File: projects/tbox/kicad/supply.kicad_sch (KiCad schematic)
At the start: 38 parts, among them J2501 PWR IN (panel Powerpole), U2501 ADP7142AUJZ-5.0, U2502 OPA1678, U2503 TPS7A4701, U2504 TPS3808G01

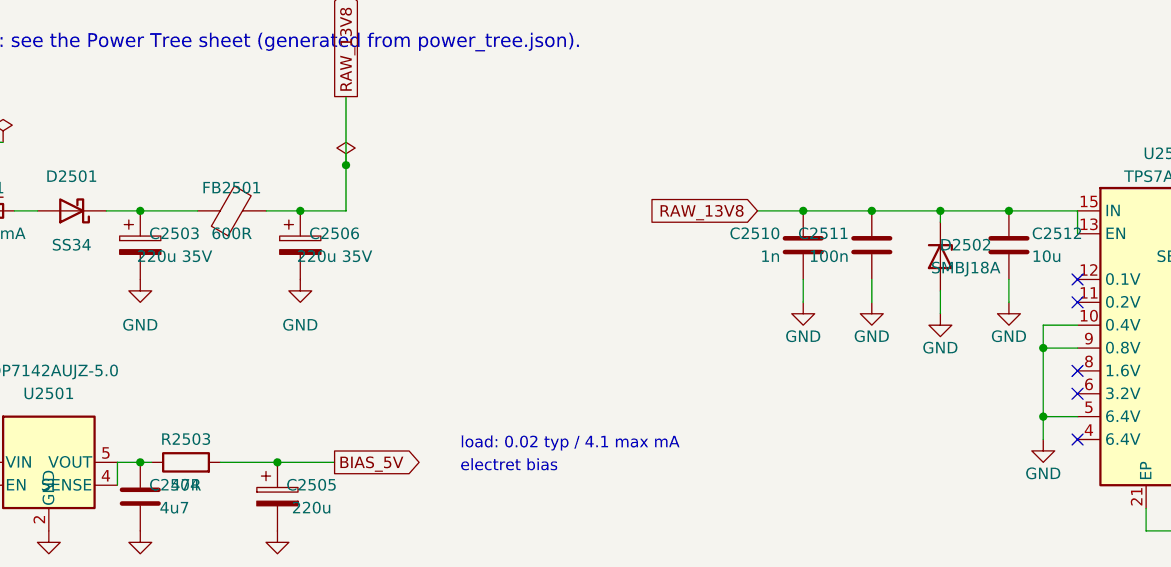
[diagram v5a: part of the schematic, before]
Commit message: Review 2 design decisions: mute cell sequencing, phones precharge, non-inverting BLEND, chassis RF returns, SP724 bypass and placement, TVS ahead of the bead, load and level updates
Q1  Mute cell: MUTE is a source-only OR with a 100k pull-down; a 2N7002
    inverter (Q1203) and sink (Q1204) pull SW_CTL hard low on release so
    the SPDT reconnects under the shunt, the fade gate charges through
    D1201/47k and bleeds through 470k (~50 ms); nothing discharges
    through MUTE any more.
Q2  1k from Vref on each OPA1622 output node (R2425-R2428) precharges
    the 470u phones caps during the hold.
Q3  Fade resistor 220R (all three instances): 0.2 dB insertion, TX_MIX
    level within 0.3 dB of the line-out jumpering.
Q4  LO stays +28 dB; -28 dBV desk mics declared out of scope in LEVELS.
Q5  SP724s stay on the rails, each with its own 100n (C1110/C1111/C1007/
    C3208 + B copies), placed behind their jack (place_panel ATTACH,
    check_placement 20 mm rule); mic RF caps C1101/C1109 return to
    CHASSIS.
Q6  Supply source envelope documented (bench/rig PSU, fused at source);
    SMBJ18A moved to the post-Schottky node ahead of FB2501; TODO for
    mobile use.
Q7  BLEND is a non-inverting summer (22k/22k into +IN, R3319 22k to Vref
    for a gain of 2), in phase with the RX selections.
Q8  Key-inhibit delay through MUTE_HOLD accepted and documented.
Q9  Beads are Murata BLM21PG601SN1D (600 R, 1.4 A, 0.14 R; datasheet
    added); PVA ordering code TODO names the panel gap that sets it.
Also: setup_pcb cuts the SJ-43514 4.5 x 1.3 mm edge notches at the jacks
on the board; supervisor hold text 1.3 s.
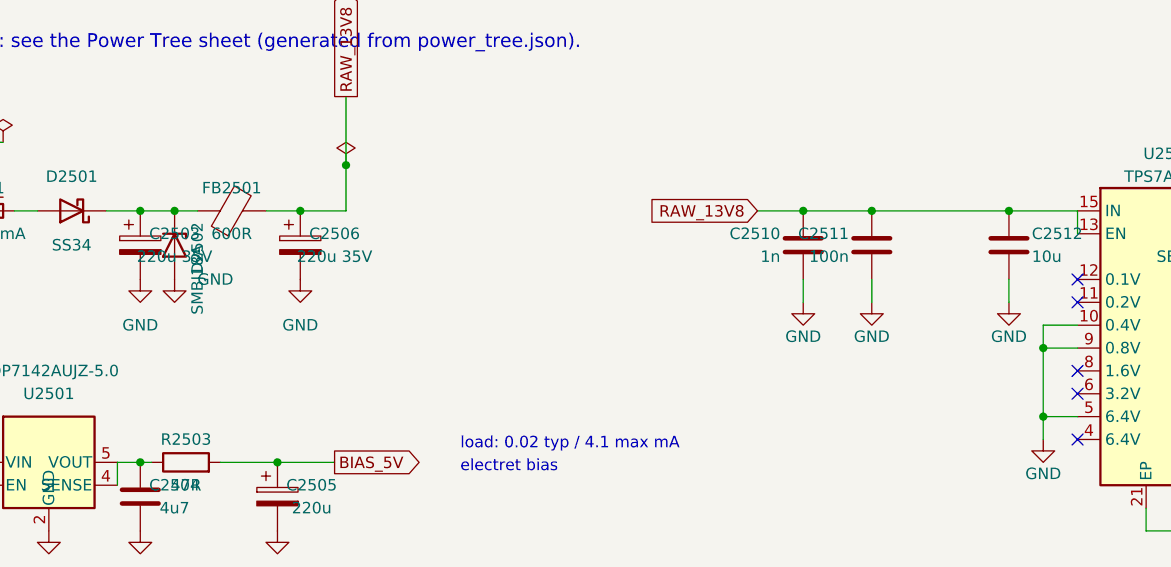
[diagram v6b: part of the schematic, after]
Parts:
- FB2501: MPN (none) -> BLM21PG601SN1D
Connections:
- net RAW_13V8: no longer D2502.1 (K)
- net at C2503.1, D2501.1 (K), FB2501.1: now also D2502.1 (K)
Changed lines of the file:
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@@
 	(wire
 		(pts
-			(xy 144.78 50.8) (xy 144.78 52.07)
-		)
-		(stroke
-			(width 0)
-			(type default)
-		)
-	)
-	(wire
-		(pts
 			(xy 180.34 55.88) (xy 182.88 55.88)
 		)
@@
 	(wire
 		(pts
-			(xy 144.78 59.69) (xy 144.78 62.23)
-		)
-		(stroke
-			(width 0)
-			(type default)
-		)
-	)
-	(wire
-		(pts
 			(xy 38.1 78.74) (xy 38.1 81.28)
 		)
@@
 	)
 	(symbol
-		(lib_id "Device:D_Zener")
-		(at 144.78 55.88 270)
-		(unit 1)
-		(body_style 1)
-		(exclude_from_sim no)
-		(in_bom yes)
-		(on_board yes)
-		(in_pos_files yes)
-		(dnp no)
-		(property "Reference" "D2502"
-			(at 147.6 54.61 90)
-			(show_name no)
-			(do_not_autoplace no)
-			(effects
-				(font
-					(size 1.27 1.27)
-				)
-			)
-		)
-		(property "Value" "SMBJ18A"
-			(at 147.6 57.15 90)
-			(show_name no)
-			(do_not_autoplace no)
-			(effects
-				(font
-					(size 1.27 1.27)
-				)
-			)
-		)
-		(property "Footprint" "Diode_SMD:D_SMB"
-			(at 144.78 55.88 0)
-			(hide yes)
-			(show_name no)
-			(do_not_autoplace no)
-			(effects
-				(font
-					(size 1.27 1.27)
-				)
-			)
-		)
-		(property "Datasheet" ""
-			(at 144.78 55.88 0)
-			(hide yes)
-			(show_name no)
-			(do_not_autoplace no)
-			(effects
-				(font
-					(size 1.27 1.27)
-				)
-			)
-		)
-		(property "Description" ""
-			(at 144.78 55.88 0)
-			(hide yes)
-			(show_name no)
-			(do_not_autoplace no)
-			(effects
-				(font
-					(size 1.27 1.27)
-				)
-			)
-		)
-		(property "MPN" "SMBJ18A"
-			(at 144.78 55.88 0)
-			(hide yes)
-			(show_name no)
-			(do_not_autoplace no)
-			(effects
-				(font
-					(size 1.27 1.27)
-				)
-			)
-		)
-		(pin "1"
-		)
-		(pin "2"
-		)
-		(instances
-			(project "tbox"
-				(path "/6a29b3f1-3e67-482d-942d-4557fa8bc2d6/7885f5d1-bf3d-5361-a0a2-98a329efbaa8/ec376872-0fd3-415b-977e-2d7984375c54"
-					(reference "D2502")
-					(unit 1)
-				)
-			)
-		)
-	)
-	(symbol
 		(lib_id "power:GND")
 		(at 55.88 58.42 0)
@@
 			)
 		)
+		(property "MPN" "BLM21PG601SN1D"
+			(at 66.04 50.8 0)
+			(show_name no)
+			(do_not_autoplace no)
+			(hide yes)
+			(effects
+				(font
+					(size 1.27 1.27)
+				)
+			)
+		)
 		(property "Footprint" "Inductor_SMD:L_0805_2012Metric"
 			(at 66.04 50.8 0)
@@
 	(symbol
 		(lib_id "power:GND")
-		(at 144.78 62.23 0)
-		(unit 1)
-		(body_style 1)
-		(exclude_from_sim no)
-		(in_bom yes)
-		(on_board yes)
-		(in_pos_files yes)
-		(dnp no)
-		(property "Reference" "#PWR02520"
-			(at 144.78 64.77 0)
-			(hide yes)
-			(show_name no)
-			(do_not_autoplace no)
-			(effects
-				(font
-					(size 1.27 1.27)
-				)
-			)
-		)
-		(property "Value" "GND"
-			(at 144.78 66.04 0)
-			(show_name no)
-			(do_not_autoplace no)
-			(effects
-				(font
-					(size 1.27 1.27)
-				)
-			)
-		)
-		(property "Footprint" ""
-			(at 144.78 62.23 0)
-			(hide yes)
-			(show_name no)
-			(do_not_autoplace no)
-			(effects
-				(font
-					(size 1.27 1.27)
-				)
-			)
-		)
-		(property "Datasheet" ""
-			(at 144.78 62.23 0)
-			(hide yes)
-			(show_name no)
-			(do_not_autoplace no)
-			(effects
-				(font
-					(size 1.27 1.27)
-				)
-			)
-		)
-		(property "Description" ""
-			(at 144.78 62.23 0)
-			(hide yes)
-			(show_name no)
-			(do_not_autoplace no)
-			(effects
-				(font
-					(size 1.27 1.27)
-				)
-			)
-		)
-		(pin "1"
-		)
-		(instances
-			(project "tbox"
-				(path "/6a29b3f1-3e67-482d-942d-4557fa8bc2d6/7885f5d1-bf3d-5361-a0a2-98a329efbaa8/ec376872-0fd3-415b-977e-2d7984375c54"
-					(reference "#PWR02520")
-					(unit 1)
-				)
-			)
-		)
-	)
-	(symbol
-		(lib_id "power:GND")
 		(at 129.54 60.96 0)
 		(unit 1)
@@
 	)
 	(junction
-		(at 144.78 50.8)
-		(diameter 0)
-		(color 0 0 0 0)
-	)
-	(junction
 		(at 152.4 50.8)
 		(diameter 0)
@@
   (text "load: 0.02 typ / 4.1 max mA" (exclude_from_sim no) (at 91.44 77.47 0) (effects (font (size 1.27 1.27)) (justify left bottom)))
   (text "DC bias only, no load by design" (exclude_from_sim no) (at 73.66 125.73 0) (effects (font (size 1.27 1.27)) (justify left bottom)))
+	(symbol
+		(lib_id "Device:D_Zener")
+		(at 59.69 54.61 270)
+		(unit 1)
+		(exclude_from_sim no)
+		(in_bom yes)
+		(on_board yes)
+		(dnp no)
+		(property "Reference" "D2502"
+			(at 62.23 52.07 0)
+			(show_name no)
+			(do_not_autoplace no)
+			(effects
+				(font
+					(size 1.27 1.27)
+				)
+				(justify left)
+			)
+		)
+		(property "Value" "SMBJ18A"
+			(at 62.23 54.61 0)
+			(show_name no)
+			(do_not_autoplace no)
+			(effects
+				(font
+					(size 1.27 1.27)
+				)
+				(justify left)
+			)
+		)
+		(property "Footprint" "Diode_SMD:D_SMB"
+			(at 59.69 54.61 0)
+			(show_name no)
+			(do_not_autoplace no)
+			(hide yes)
+			(effects
+				(font
+					(size 1.27 1.27)
+				)
+				(justify left)
+			)
+		)
+		(property "Datasheet" ""
+			(at 59.69 54.61 0)
+			(show_name no)
+			(do_not_autoplace no)
+			(hide yes)
+			(effects
+				(font
+					(size 1.27 1.27)
+				)
+				(justify left)
+			)
+		)
+		(property "Description" ""
+			(at 59.69 54.61 0)
+			(show_name no)
+			(do_not_autoplace no)
+			(hide yes)
+			(effects
+				(font
+					(size 1.27 1.27)
+				)
+				(justify left)
+			)
+		)
+		(property "MPN" "SMBJ18A"
+			(at 59.69 54.61 0)
+			(show_name no)
+			(do_not_autoplace no)
+			(hide yes)
+			(effects
+				(font
+					(size 1.27 1.27)
+				)
+				(justify left)
+			)
+		)
+		(pin "1"
+		)
+		(pin "2"
+		)
+		(instances
+			(project "tbox"
+				(path "/6a29b3f1-3e67-482d-942d-4557fa8bc2d6/7885f5d1-bf3d-5361-a0a2-98a329efbaa8/ec376872-0fd3-415b-977e-2d7984375c54"
+					(reference "D2502")
+					(unit 1)
+				)
+			)
+		)
+	)
+	(junction
+		(at 59.69 50.8)
+		(diameter 0)
+		(color 0 0 0 0)
+	)
+	(symbol
+		(lib_id "power:GND")
+		(at 59.69 58.42 0)
+		(unit 1)
+		(exclude_from_sim no)
+		(in_bom yes)
+		(on_board yes)
+		(dnp no)
+		(property "Reference" "#PWR02520"
+			(at 62.23 55.88 0)
+			(show_name no)
+			(do_not_autoplace no)
+			(hide yes)
+			(effects
+				(font
+					(size 1.27 1.27)
+				)
+				(justify left)
+			)
+		)
+		(property "Value" "GND"
+			(at 62.23 58.42 0)
+			(show_name no)
+			(do_not_autoplace no)
+			(effects
+				(font
+					(size 1.27 1.27)
+				)
+				(justify left)
+			)
+		)
+		(property "Footprint" ""
+			(at 59.69 58.42 0)
+			(show_name no)
+			(do_not_autoplace no)
+			(hide yes)
+			(effects
+				(font
+					(size 1.27 1.27)
+				)
+				(justify left)
+			)
+		)
+		(property "Datasheet" ""
+			(at 59.69 58.42 0)
+			(show_name no)
+			(do_not_autoplace no)
+			(hide yes)
+			(effects
+				(font
+					(size 1.27 1.27)
+				)
+				(justify left)
+			)
+		)
+		(property "Description" ""
+			(at 59.69 58.42 0)
+			(show_name no)
+			(do_not_autoplace no)
+			(hide yes)
+			(effects
+				(font
+					(size 1.27 1.27)
+				)
+				(justify left)
+			)
+		)
+		(pin "1"
+		)
+		(instances
+			(project "tbox"
+				(path "/6a29b3f1-3e67-482d-942d-4557fa8bc2d6/7885f5d1-bf3d-5361-a0a2-98a329efbaa8/ec376872-0fd3-415b-977e-2d7984375c54"
+					(reference "#PWR02520")
+					(unit 1)
+				)
+			)
+		)
+	)
 )

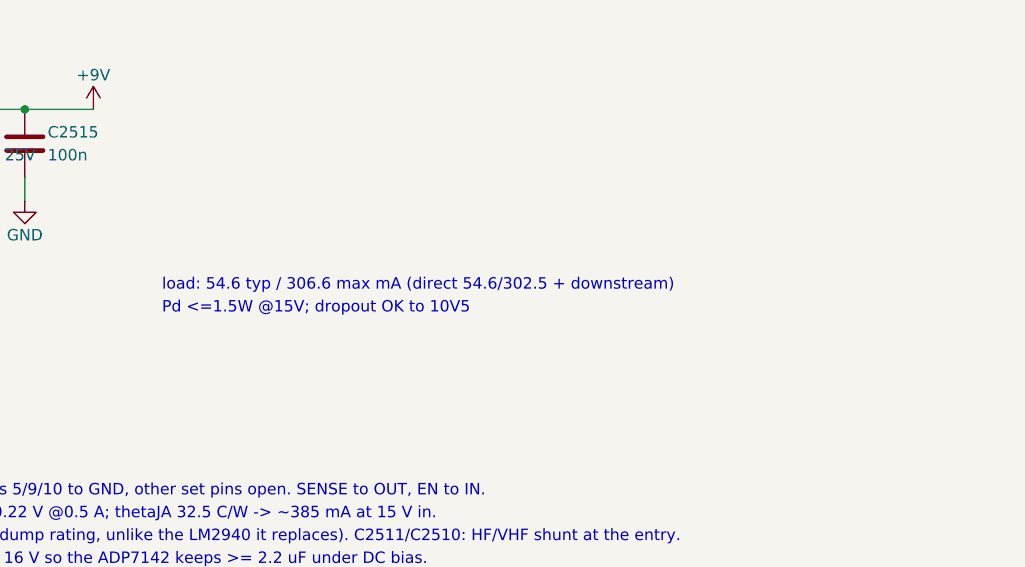
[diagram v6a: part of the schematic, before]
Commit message: Mute cell rework and a stronger supervisor pull-up (review 3, findings 4-6)
The mute command is now buffered once before it drives anything with a
capacitor on it, and both timing networks hang off that buffer:

- Q1203 (BSS138BK, Vgs(th) 0.48-1.6 V) inverts MUTE to MUTE_N; Q1204
  inverts that to MUTE_DRV, a stiff 0/+9 V copy with a 2k2 pull-up.
  Nothing can feed back into the diode-OR command line, which was what
  held MUTE at SW_CTL/2 and delayed reconnection by 101-285 ms.
- Fade gate: 4k7 + D1201 charge, 100k discharge returned to MUTE_DRV,
  470n. Both ends sit at +9 V when muted, so the gate reaches the full
  rail (4.5 V above Vref) instead of 7.0 V through the old 47k/470k
  divider and diode drop.
- Switch delay: 470k into 1u, with D1202 + 220R across it to dump the
  cap into Q1204 on release (about 1 ms at 35 mA) while the shunt still
  conducts. The 470k is chosen so even the earliest possible logic trip
  (0.8 V, the only bound the TS12A12511 gives at this supply) finds the
  shunt already conducting.
- Shunt pair is PMV30UN2, whose R_DS(on) is specified at 1.5 V of gate
  drive (100 mohm max, 43 mohm at 2.5 V): -60.8 dB against the 220R at
  brown-out drive, -70.7 dB at a healthy rail. The 2N7002 it replaces is
  specified only at 5 V and 10 V.
- R2122 100k -> 10k. Against the two channels' 100k command pull-downs
  it puts MUTE_HOLD at 7.0 V with the rail at 9 V and 4.5 V at 6 V,
  where 100k gave 2.8 V and 1.8 V against a threshold specified as high
  as 2.5 V. With the timing capacitors now behind each cell's buffer the
  key inhibit follows PWR_OK promptly instead of waiting for them.

Datasheets for both new parts added. Board synced and re-placed.
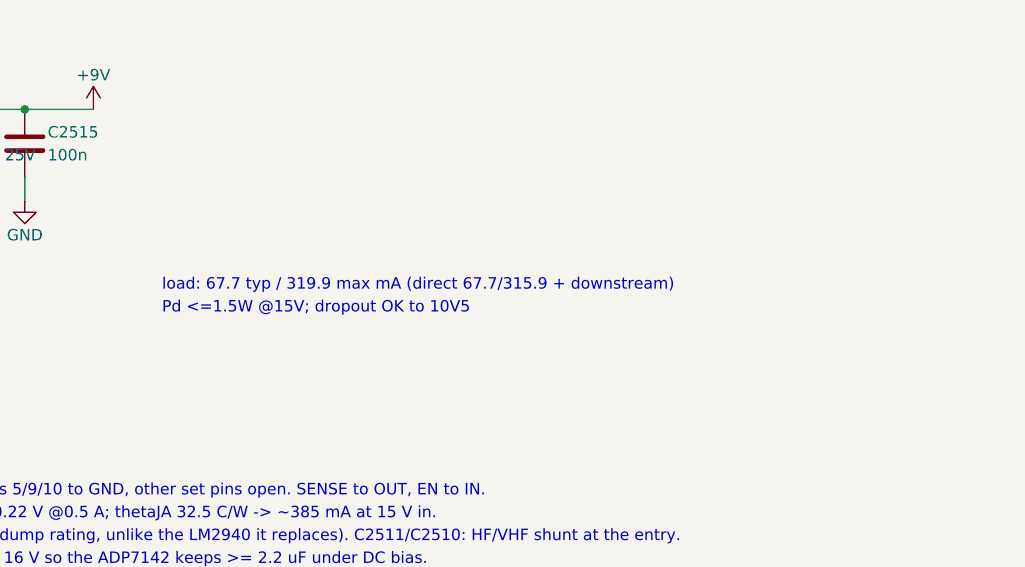
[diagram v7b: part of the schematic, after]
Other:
- note added: "load: 67.7 typ / 319.9 max mA (direct 67.7/315.9 + downstream)"
- note removed: "load: 54.6 typ / 306.6 max mA (direct 54.6/302.5 + downstream)"
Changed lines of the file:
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@@
 		)
 	)
-  (text "Pd <=1.5W @15V; dropout OK to 10V5" (exclude_from_sim no) (at 213.36 73.66 0) (effects (font (size 1.27 1.27)) (justify left bottom)))
-  (text "load: 54.6 typ / 306.6 max mA (direct 54.6/302.5 + downstream)" (exclude_from_sim no) (at 213.36 71.12 0) (effects (font (size 1.27 1.27)) (justify left bottom)))
-  (text "electret bias" (exclude_from_sim no) (at 91.44 80.01 0) (effects (font (size 1.27 1.27)) (justify left bottom)))
-  (text "load: 0.02 typ / 4.1 max mA" (exclude_from_sim no) (at 91.44 77.47 0) (effects (font (size 1.27 1.27)) (justify left bottom)))
-  (text "DC bias only, no load by design" (exclude_from_sim no) (at 73.66 125.73 0) (effects (font (size 1.27 1.27)) (justify left bottom)))
 	(symbol
 		(lib_id "Device:D_Zener")
@@
 		)
 	)
+  (text "Pd <=1.5W @15V; dropout OK to 10V5" (exclude_from_sim no) (at 213.36 73.66 0) (effects (font (size 1.27 1.27)) (justify left bottom)))
+  (text "load: 67.7 typ / 319.9 max mA (direct 67.7/315.9 + downstream)" (exclude_from_sim no) (at 213.36 71.12 0) (effects (font (size 1.27 1.27)) (justify left bottom)))
+  (text "electret bias" (exclude_from_sim no) (at 91.44 80.01 0) (effects (font (size 1.27 1.27)) (justify left bottom)))
+  (text "load: 0.02 typ / 4.1 max mA" (exclude_from_sim no) (at 91.44 77.47 0) (effects (font (size 1.27 1.27)) (justify left bottom)))
+  (text "DC bias only, no load by design" (exclude_from_sim no) (at 73.66 125.73 0) (effects (font (size 1.27 1.27)) (justify left bottom)))
 )
